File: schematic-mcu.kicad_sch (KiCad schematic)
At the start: 24 parts, among them U5 USBLC6-2P6, U6 ESP32-S3FN8, Y1 Crystal_GND24

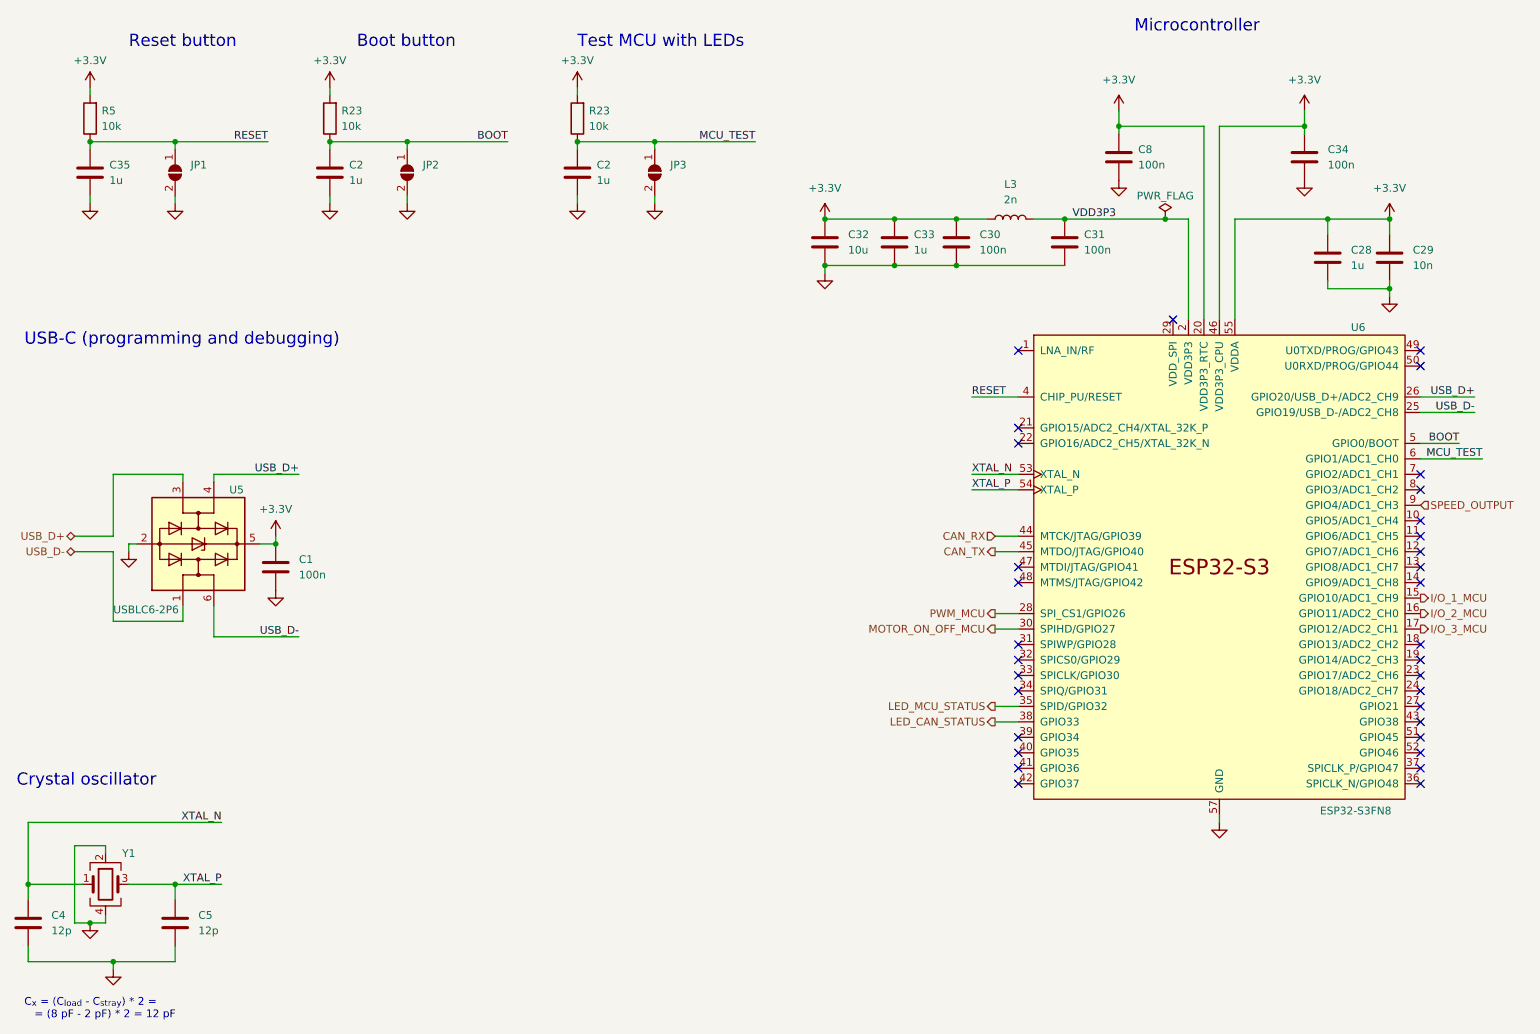
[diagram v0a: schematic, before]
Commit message: Remake motor control driver
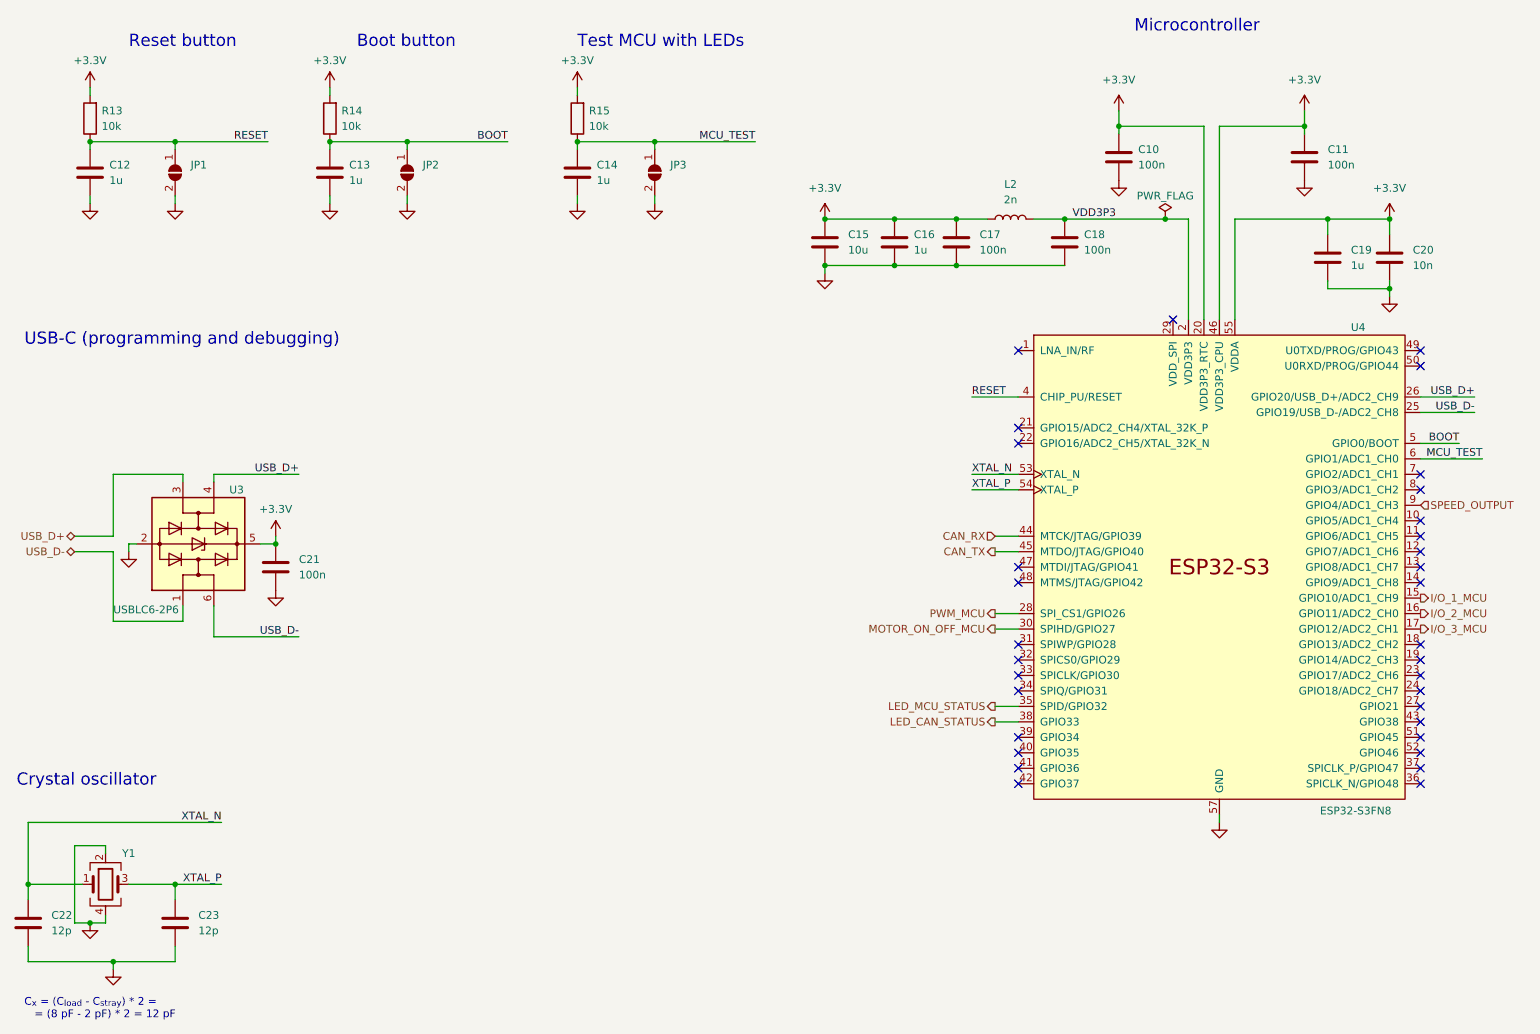
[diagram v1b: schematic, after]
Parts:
- renumbered C8 to C10, C34 to C11, C35 to C12, C2 to C13, C2 to C14, C32 to C15, C33 to C16, C30 to C17, C31 to C18, C28 to C19, C29 to C20, C1 to C21, C4 to C22, C5 to C23, L3 to L2, R5 to R13, R23 to R14, R23 to R15, U5 to U3, U6 to U4

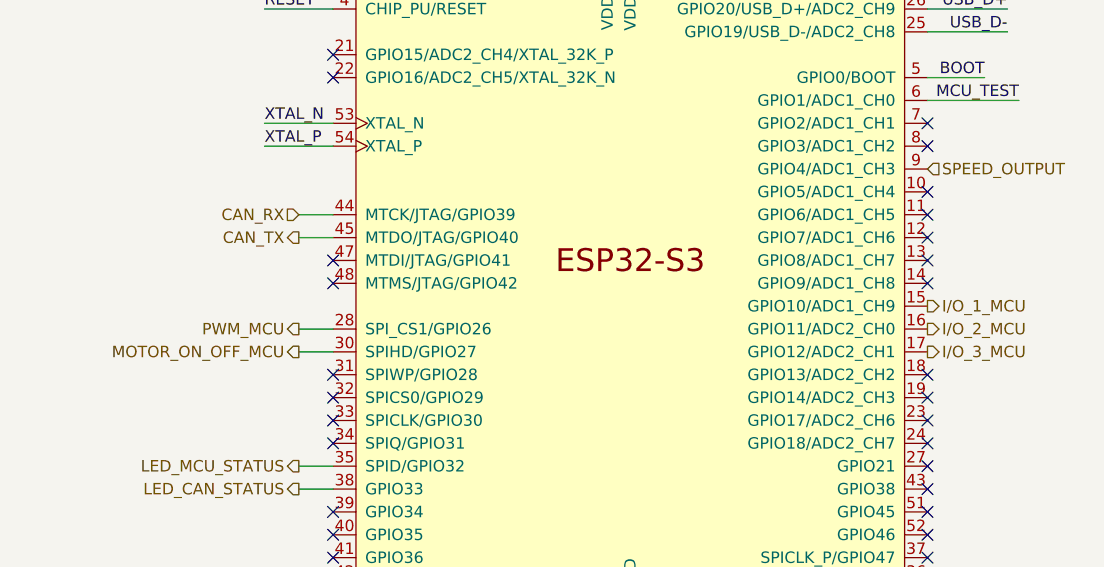
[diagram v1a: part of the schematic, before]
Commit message: Add Emergency button option
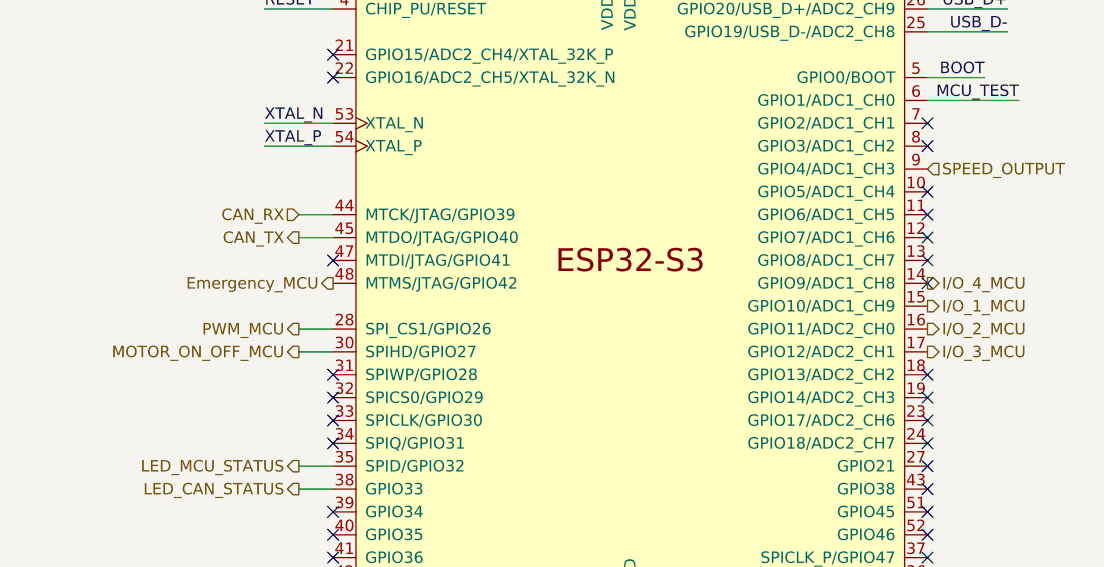
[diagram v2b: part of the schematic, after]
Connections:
- net I/O_4_MCU: now reaches U4.14 (GPIO9/ADC1_CH8)
- net Emergency_MCU: now reaches U4.48 (MTMS/JTAG/GPIO42)
- no-connect marks 33 -> 32
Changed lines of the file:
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@@
-	)
-	(no_connect
-		(at 195.58 113.03)
 	)
 	(no_connect
@@
 		)
 	)
+	(hierarchical_label "Emergency_MCU"
+		(shape output)
+		(at 195.58 113.03 180)
+		(fields_autoplaced yes)
+		(effects
+			(font
+				(size 1.27 1.27)
+			)
+			(justify right)
+		)
+	)
 	(hierarchical_label "MOTOR_ON_OFF_MCU"
 		(shape output)
@@
 		)
 	)
+	(hierarchical_label "I{slash}O_4_MCU"
+		(shape output)
+		(at 261.62 113.03 0)
+		(fields_autoplaced yes)
+		(effects
+			(font
+				(size 1.27 1.27)
+			)
+			(justify left)
+		)
+	)

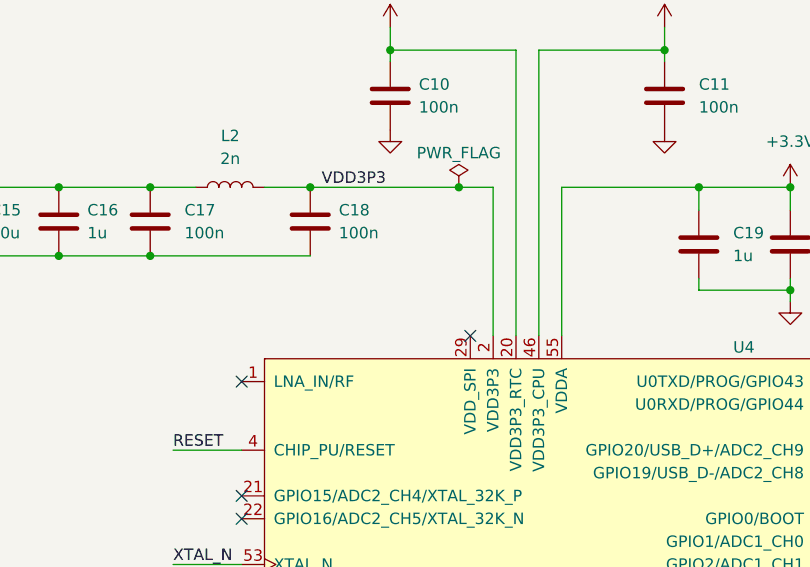
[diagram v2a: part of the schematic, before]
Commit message: Repair fedback capacitor 3.3V regulator
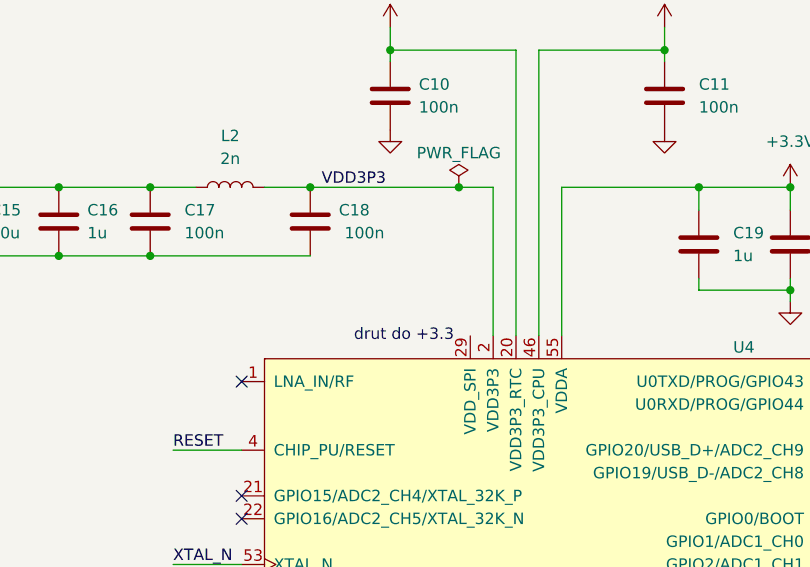
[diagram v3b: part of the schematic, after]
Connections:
- no-connect marks 32 -> 31
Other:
- note added: "drut do +3.3"
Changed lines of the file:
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@@
 	)
 	(no_connect
-		(at 220.98 69.85)
-	)
-	(no_connect
 		(at 195.58 123.19)
 	)
@@
 		)
 	)
+	(text "drut do +3.3"
+		(exclude_from_sim no)
+		(at 213.614 69.85 0)
+		(effects
+			(font
+				(size 1.27 1.27)
+			)
+		)
+	)
 	(text "Boot button"
 		(exclude_from_sim no)
@@
 		(on_board yes)
 		(dnp no)
-		(fields_autoplaced yes)
 		(property "Reference" "C18"
 			(at 206.375 55.8799 0)
@@
 		)
 		(property "Value" "100n"
-			(at 206.375 58.4199 0)
+			(at 207.01 58.42 0)
 			(effects
 				(font
